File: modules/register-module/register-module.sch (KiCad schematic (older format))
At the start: 42 parts, among them U1 74HC04, U10 74HC574, U11 74HC574, U12 74HC574, U13 74HC161, U14 74HC161, U15 74HC161, U16 74HC161, U17 74HC245, U18 74HC245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

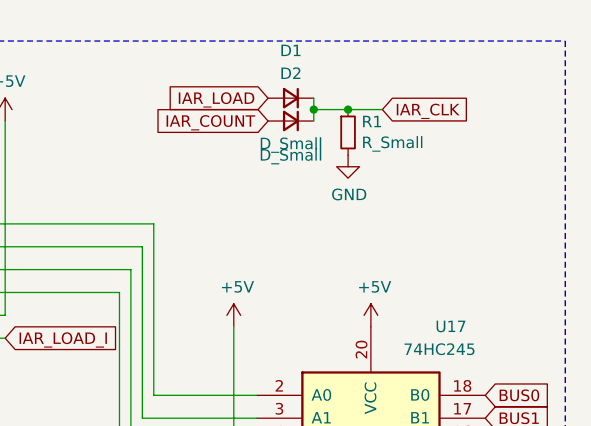
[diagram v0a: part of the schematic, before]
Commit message: changed the mask clearance for plotting
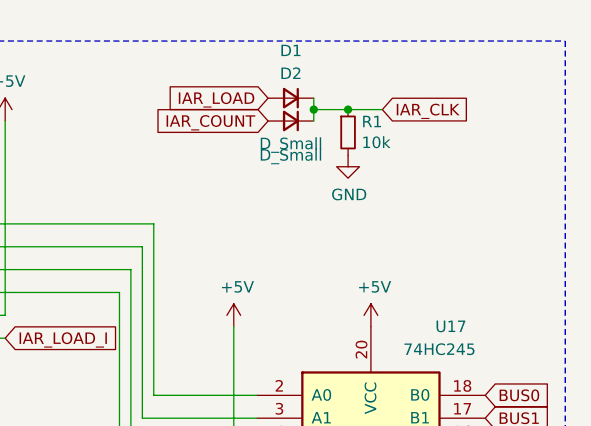
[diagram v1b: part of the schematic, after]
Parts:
- R1: value R_Small -> 10k
